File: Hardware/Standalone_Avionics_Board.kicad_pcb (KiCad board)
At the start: 4 copper layers, 184.3 x 25.4 mm, 136 parts, among them J1 GPS_Ant, J2 Charges A/B Terminal, J3 Charges C/D Terminal, J4 RF_Ant, J5 3-Pin Molex Power, J6 10118192-0001LF, J7 ARM 10 Pin, Q1 SI1040X-T1-GE3, Q2 SI7232DN-T1-GE3, Q3 SI7232DN-T1-GE3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

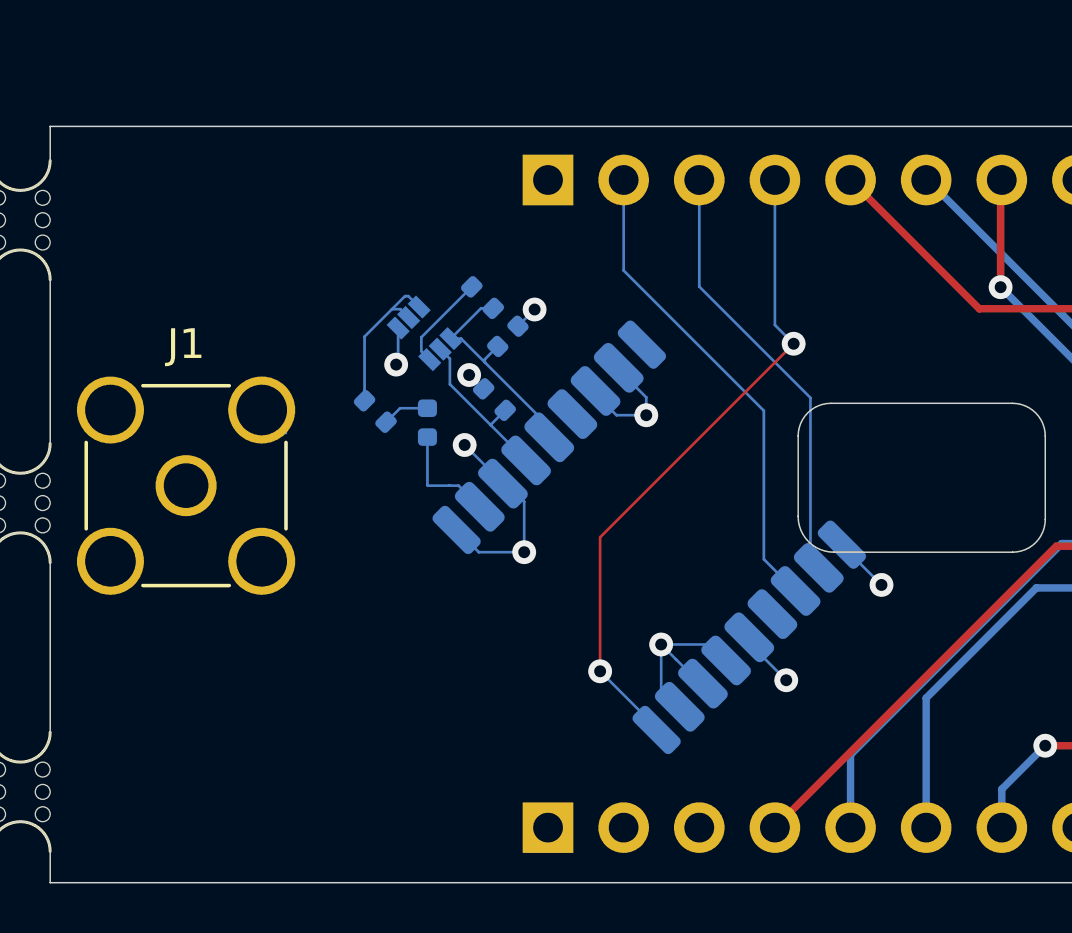
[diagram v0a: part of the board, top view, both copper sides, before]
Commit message: Adjusted GPS module position
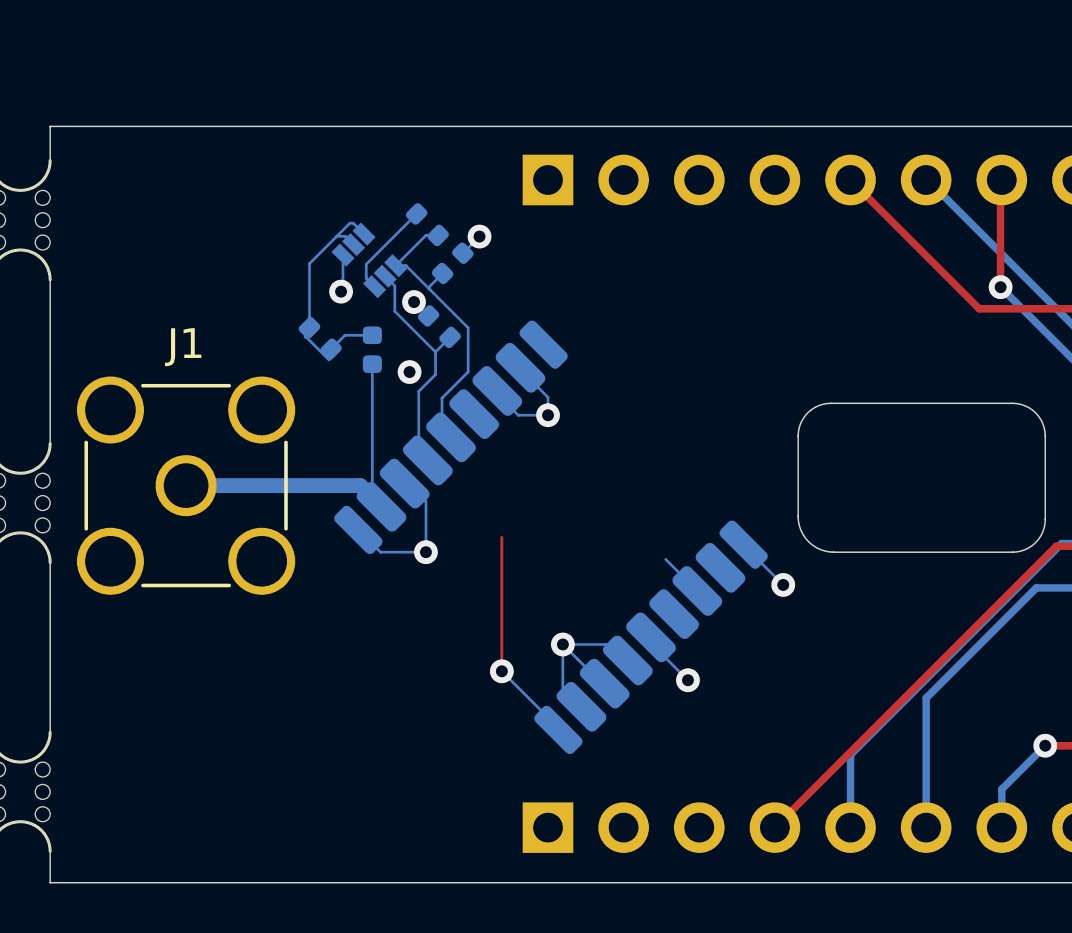
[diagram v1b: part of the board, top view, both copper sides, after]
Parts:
- moved U6 3.30 mm to (192.6, 123.8)
- moved L12 3.07 mm to (186.6, 117.5)
- moved Q1 3.07 mm to (186.5, 114.5)
- moved R2 3.07 mm to (184.9, 117.2)
- moved R4 3.07 mm to (188.5, 113.3)
- moved C23 3.07 mm to (189.3, 114.7)
- moved R3 3.07 mm to (188.9, 116.8)
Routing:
- net /~GPS_RESET: track 38.5 -> 23.5 mm, vias 2 -> 1
- net /GPS_RX: track 36.5 -> 21.8 mm
- net /GPS_TX: track 32.7 -> 18.4 mm
- net /MAX-8Q/GPS_ANT: track 3.68 -> 11.8 mm
- net /MAX-8Q/GPS_VCC_RF: track 7.46 -> 10.5 mm
- net GND: track 102.4 -> 99.5 mm
- net /MAX-8Q/GPS_LNA_EN: track 5.63 -> 8.04 mm
- net Net-(Q1-Pad2): track 5.74 -> 6.87 mm
- added copper zone on 3v3.Cu, net +3V3

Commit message: Connected SPI lines to RX/TX chips
Really need to figure out layout for crystals
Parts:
- moved Y1 6.60 mm to (108.2, 116.0), turned to 0 degrees
- moved Y2 6.47 mm to (108.2, 129.6), turned to 0 degrees
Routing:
- net /~RX_SEL: track 0.00 -> 57.1 mm, vias 0 -> 2
- net /TX_SCL: track 0.00 -> 46.3 mm, vias 0 -> 2
- net /TX_SDO: track 0.00 -> 44.3 mm, vias 0 -> 2
- net /~RX_IRQ: track 0.00 -> 43.4 mm, vias 0 -> 4
- net /TX_SDI: track 0.00 -> 43.2 mm, vias 0 -> 2
- net /RX_SCL: track 0.00 -> 40.9 mm, vias 0 -> 2
- net /RX_SDO: track 0.00 -> 40.3 mm, vias 0 -> 2
- net /~TX_IRQ: track 0.00 -> 36.9 mm, vias 0 -> 4
- net /~TX_SEL: track 0.00 -> 36.0 mm, vias 0 -> 2
- net /RX_SDI: track 0.00 -> 35.9 mm, vias 0 -> 2
- net Net-(U2-Pad17): track 0.00 -> 15.7 mm
- net Net-(U1-Pad17): track 0.00 -> 15.7 mm
- net Net-(U2-Pad16): track 0.00 -> 13.9 mm
- net Net-(U1-Pad16): track 0.00 -> 10.9 mm
- net +5V: track 143.8 -> 145.2 mm
